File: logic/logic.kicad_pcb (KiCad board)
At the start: 2 copper layers, 32 parts, among them J1 DIN41612_03x32_ABC, J2 Conn_02x05_Odd_Even, J3 Conn_02x05_Odd_Even, J4 Conn_02x05_Odd_Even, U1 TPIC6595, U11 LM7805_TO220, U2 TPIC6595, U3 TPIC6595, U4 TPIC6595, U5 TPIC6595, U6 TPIC6595, U7 TPIC6595, U8 TPIC6595, U9 74HC14

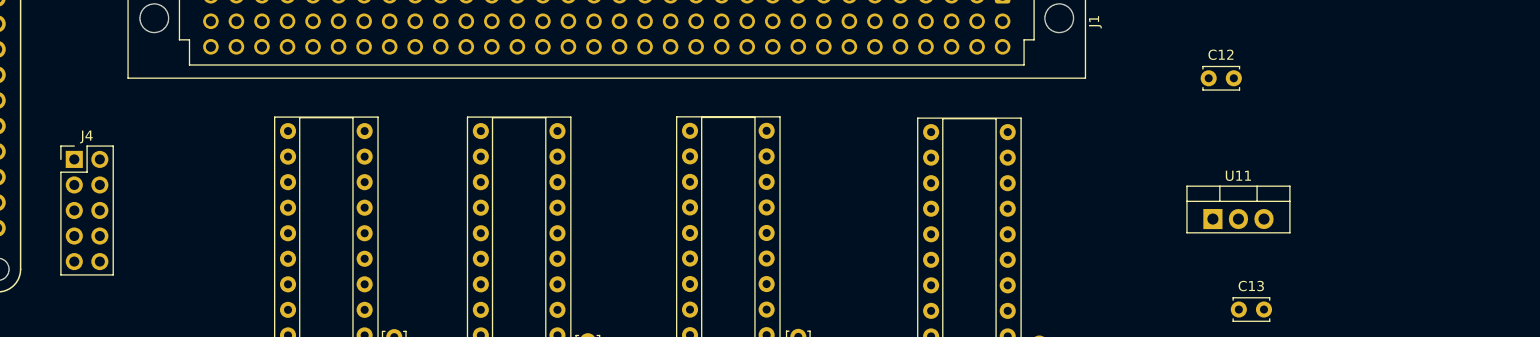
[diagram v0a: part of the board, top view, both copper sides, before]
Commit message: Update libraries, schematic, and layout with buck converter
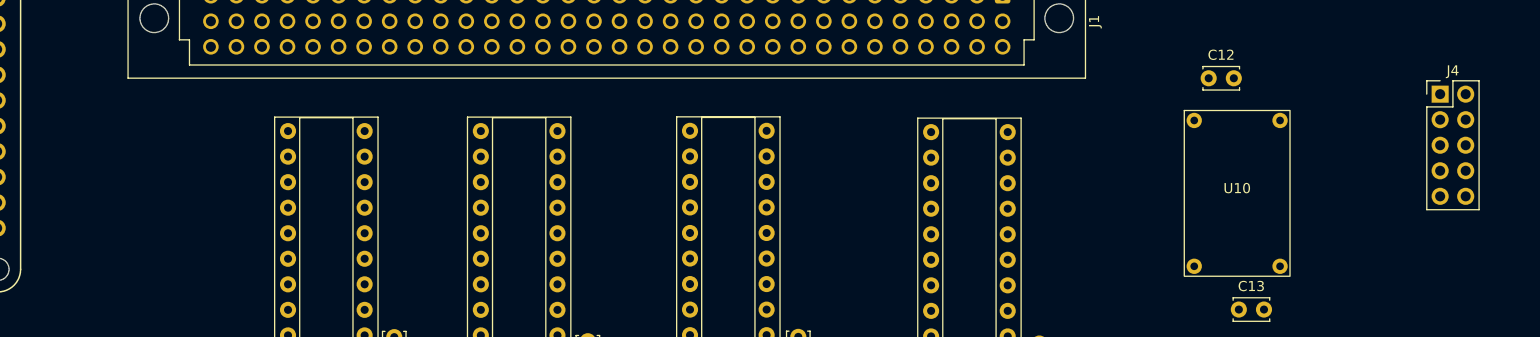
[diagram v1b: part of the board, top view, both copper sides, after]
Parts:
- removed U11: LM7805_TO220, Package_TO_SOT_THT:TO-220-3_Vertical
- added U10: ~, NixComp:TR4R7, F.Cu at (217.3, 90.5)
- moved J4 136.0 mm to (237.5, 80.6)

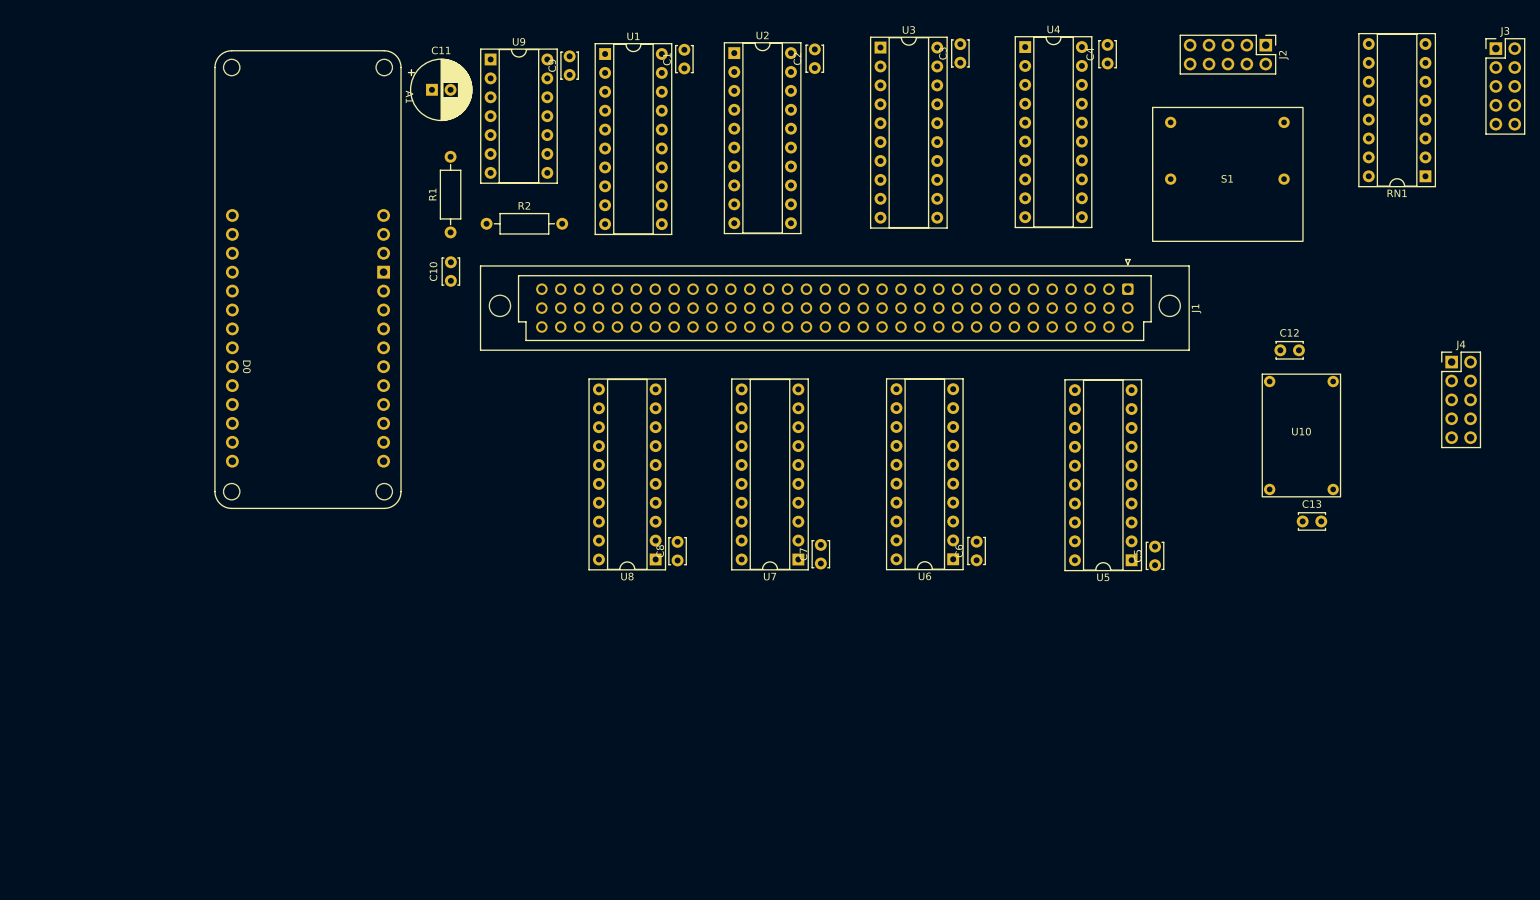
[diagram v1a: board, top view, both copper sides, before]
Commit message: Complete schematic and begin logic board layout.
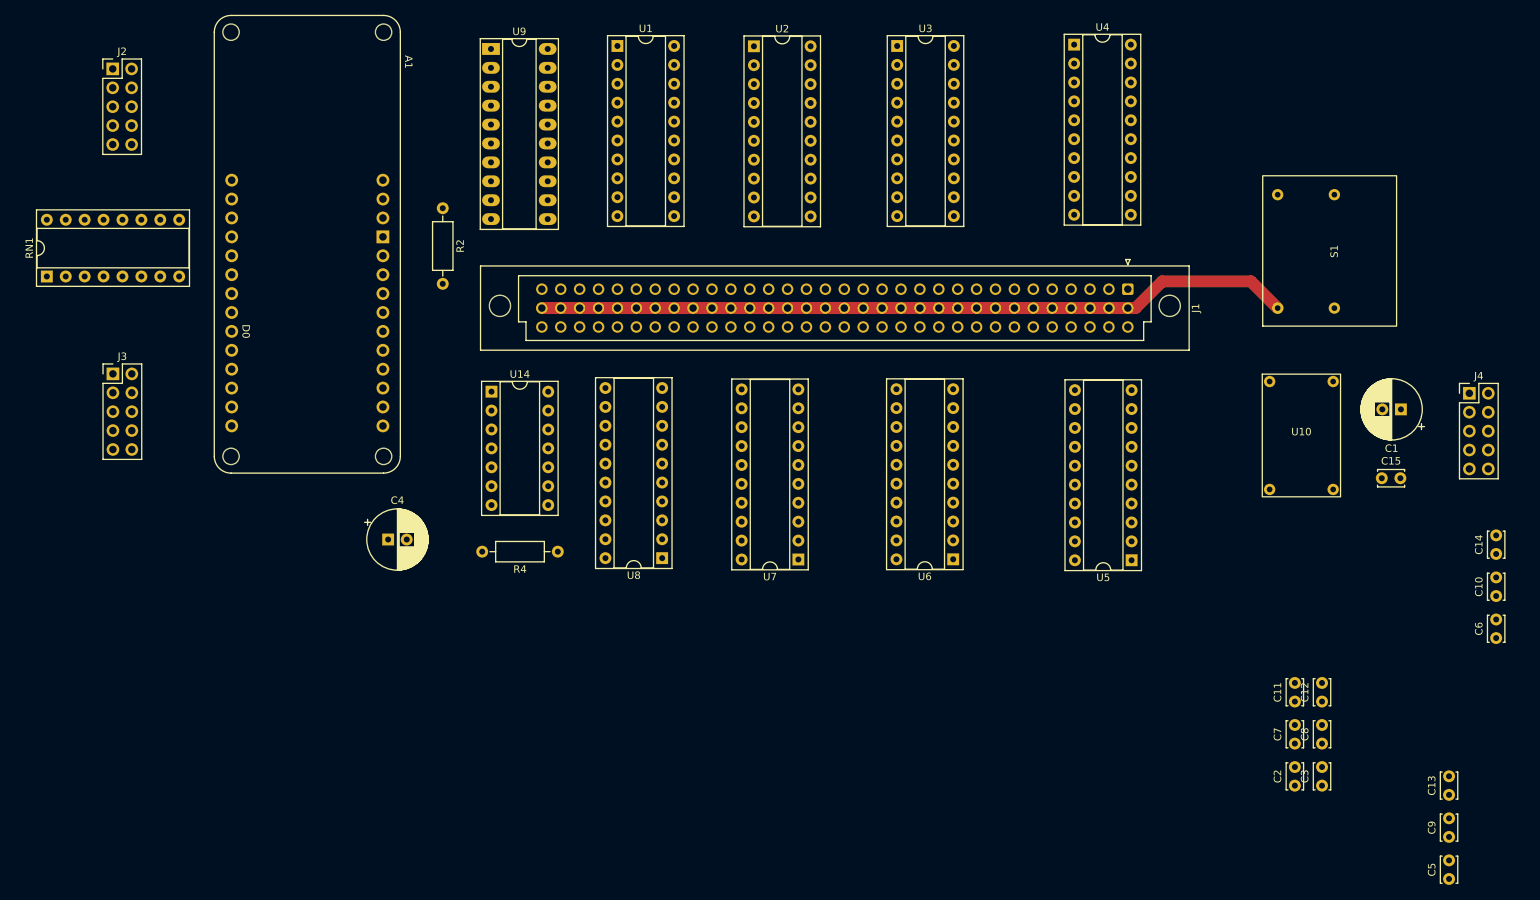
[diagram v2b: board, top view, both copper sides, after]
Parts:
- removed R1: R, Resistor_THT:R_Axial_DIN0207_L6.3mm_D2.5mm_P10.16mm_Horizontal
- added C14: C, Capacitor_THT:C_Disc_D3.4mm_W2.1mm_P2.50mm, F.Cu at (243.5, 106.4)
- added C15: C, Capacitor_THT:C_Disc_D3.4mm_W2.1mm_P2.50mm, F.Cu at (228.1, 96.2)
- added R4: R, Resistor_THT:R_Axial_DIN0207_L6.3mm_D2.5mm_P10.16mm_Horizontal, F.Cu at (117.4, 106.1)
- added U14: 74HC14, Package_DIP:DIP-14_W7.62mm_Socket, F.Cu at (108.5, 84.6)
- C1, C4: footprint Capacitor_THT:C_Disc_D3.4mm_W2.1mm_P2.50mm -> Capacitor_THT:CP_Radial_D8.0mm_P2.50mm
- C11: footprint Capacitor_THT:CP_Radial_D8.0mm_P2.50mm -> Capacitor_THT:C_Disc_D3.4mm_W2.1mm_P2.50mm
- U9: value 74HC14 -> 74HCT244; footprint Package_DIP:DIP-14_W7.62mm_Socket -> Package_DIP:DIP-20_W7.62mm_Socket_LongPads
- moved J3 190.9 mm to (57.6, 82.2)
- moved RN1 185.7 mm to (48.8, 69.1), turned to 90 degrees
- moved C9 156.4 mm to (237.2, 144.4)
- moved J2 155.0 mm to (57.6, 41.2), turned to 0 degrees
- moved C10 146.7 mm to (243.5, 112.0)
- moved C11 142.1 mm to (216.4, 126.2), turned to 90 degrees
- moved C2 116.0 mm to (216.4, 137.5)
- moved C4 115.9 mm to (94.6, 104.4), turned to 0 degrees
- moved C3 108.6 mm to (220.1, 137.5)
- moved C1 106.6 mm to (230.7, 86.9), turned to 180 degrees
- moved C8 90.0 mm to (220.1, 131.8)
- moved C6 70.6 mm to (243.5, 117.7)
- moved C7 68.1 mm to (216.4, 131.8)
- moved C5 57.8 mm to (237.2, 150.0)
- moved C12 47.5 mm to (220.1, 126.2), turned to 90 degrees
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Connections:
- A1 pad 3V3: unconnected-(A1-3.3V-Pad3V3) -> V3.3
- A1 pad 5V: VCC -> unconnected-(A1-Pad5V)
- A1 pad A1: /BT1 -> /~{SRCLR3.3}
- A1 pad A2: /BT2 -> Net-(J2-Pin_1)
- A1 pad A3: /SPARE1 -> Net-(J2-Pin_3)
- A1 pad A4: /SPARE2 -> Net-(J2-Pin_5)
- A1 pad A5: /SW1 -> Net-(J2-Pin_7)
- A1 pad A6: /SW2 -> Net-(J2-Pin_9)
- A1 pad D0: Net-(RN1-R6.1) -> Net-(RN1-R8.1)
- A1 pad D1: Net-(RN1-R5.1) -> Net-(RN1-R7.1)
- A1 pad D2: Net-(RN1-R4.1) -> Net-(RN1-R6.1)
- A1 pad D3: Net-(RN1-R3.1) -> Net-(RN1-R5.1)
- A1 pad D4: Net-(RN1-R2.1) -> Net-(RN1-R4.1)
- A1 pad D5: Net-(RN1-R1.1) -> Net-(RN1-R3.1)
- A1 pad D7: /RCLK -> Net-(U9-I0a)
- A1 pad D8: /COPI -> Net-(A1-D8_MOSI)
- A1 pad D9: /SRCK -> Net-(A1-D9_SCK)
- A1 pad VIN: LV_REG -> V5.0
- C1 pad 1: GND -> Net-(J4-Pin_10)
- C1 pad 2: VCC -> GND
- C10 pad 1: GND -> V5.0
- C10 pad 2: VCC -> GND
- C11 pad 1: Net-(C11-Pad1) -> V5.0
- C12 pad 1: Net-(J4-Pin_10) -> V5.0
- C13 pad 1: LV_REG -> V5.0
- C2 pad 1: GND -> Net-(J4-Pin_10)
- C2 pad 2: VCC -> GND
- C3 pad 1: GND -> V5.0
- C3 pad 2: VCC -> GND
- C4 pad 1: GND -> Net-(C4-Pad1)
- C4 pad 2: VCC -> GND
- C5 pad 1: GND -> V5.0
- C5 pad 2: VCC -> GND
- C6 pad 1: GND -> V5.0
- C6 pad 2: VCC -> GND
- C7 pad 1: GND -> V5.0
- C7 pad 2: VCC -> GND
- C8 pad 1: GND -> V5.0
- C8 pad 2: VCC -> GND
- C9 pad 1: GND -> V5.0
- C9 pad 2: VCC -> GND
- J1 pad a1: unconnected-(J1-Pin_a1-Pada1) -> /B4-0
- J1 pad a10: /B3-6 -> /B3-1
- J1 pad a11: /B3-5 -> /B3-2
- J1 pad a12: /B3-4 -> /B3-3
- J1 pad a13: /B3-3 -> /B3-4
- J1 pad a14: /B3-2 -> /B3-5
- J1 pad a15: /B3-1 -> /B3-6
- J1 pad a16: /B3-0 -> /B3-7
- J1 pad a17: /B2-7 -> /B2-0
- J1 pad a18: /B2-6 -> /B2-1
- J1 pad a19: /B2-5 -> /B2-2
- J1 pad a2: unconnected-(J1-Pin_a2-Pada2) -> /B4-1
- J1 pad a20: /B2-4 -> /B2-3
- J1 pad a21: /B2-3 -> /B2-4
- J1 pad a22: /B2-2 -> /B2-5
- J1 pad a23: /B2-1 -> /B2-6
- J1 pad a24: /B2-0 -> /B2-7
- J1 pad a25: /B1-7 -> /B1-0
- J1 pad a26: /B1-6 -> /B1-1
- J1 pad a27: /B1-5 -> /B1-2
- J1 pad a28: /B1-4 -> /B1-3
- J1 pad a29: /B1-3 -> /B1-4
- J1 pad a3: /B4-5 -> /B4-2
- J1 pad a30: /B1-2 -> /B1-5
- J1 pad a31: /B1-1 -> /B1-6
- J1 pad a32: /B1-0 -> /B1-7
- J1 pad a4: /B4-4 -> /B4-3
- J1 pad a5: /B4-3 -> /B4-4
- J1 pad a6: /B4-2 -> /B4-5
- J1 pad a7: /B4-1 -> /B4-6
- J1 pad a8: /B4-0 -> /B4-7
- J1 pad a9: /B3-7 -> /B3-0
- J1 pad b1: Net-(J1-Pin_b1) -> V170
- J1 pad b10: Net-(J1-Pin_b1) -> V170
- J1 pad b11: Net-(J1-Pin_b1) -> V170
- J1 pad b12: Net-(J1-Pin_b1) -> V170
- J1 pad b13: Net-(J1-Pin_b1) -> V170
- J1 pad b14: Net-(J1-Pin_b1) -> V170
- J1 pad b15: Net-(J1-Pin_b1) -> V170
- J1 pad b16: Net-(J1-Pin_b1) -> V170
- J1 pad b17: Net-(J1-Pin_b1) -> V170
- J1 pad b18: Net-(J1-Pin_b1) -> V170
- J1 pad b19: Net-(J1-Pin_b1) -> V170
- J1 pad b2: Net-(J1-Pin_b1) -> V170
- J1 pad b20: Net-(J1-Pin_b1) -> V170
- J1 pad b21: Net-(J1-Pin_b1) -> V170
- J1 pad b22: Net-(J1-Pin_b1) -> V170
- J1 pad b23: Net-(J1-Pin_b1) -> V170
- J1 pad b24: Net-(J1-Pin_b1) -> V170
- J1 pad b25: Net-(J1-Pin_b1) -> V170
- J1 pad b26: Net-(J1-Pin_b1) -> V170
- J1 pad b27: Net-(J1-Pin_b1) -> V170
- J1 pad b28: Net-(J1-Pin_b1) -> V170
- J1 pad b29: Net-(J1-Pin_b1) -> V170
- J1 pad b3: Net-(J1-Pin_b1) -> V170
- J1 pad b30: Net-(J1-Pin_b1) -> V170
- J1 pad b31: Net-(J1-Pin_b1) -> V170
- J1 pad b32: Net-(J1-Pin_b1) -> V170
- J1 pad b4: Net-(J1-Pin_b1) -> V170
- J1 pad b5: Net-(J1-Pin_b1) -> V170
- J1 pad b6: Net-(J1-Pin_b1) -> V170
- J1 pad b7: Net-(J1-Pin_b1) -> V170
- J1 pad b8: Net-(J1-Pin_b1) -> V170
- J1 pad b9: Net-(J1-Pin_b1) -> V170
- J1 pad c31: unconnected-(J1-Pin_c31-Padc31) -> /B8-6
- J1 pad c32: unconnected-(J1-Pin_c32-Padc32) -> /B8-7
- J2 pad 1: VCC -> Net-(J2-Pin_1)
- J2 pad 10: /SPARE2 -> GND
- J2 pad 3: VCC -> Net-(J2-Pin_3)
- J2 pad 5: /BT1 -> Net-(J2-Pin_5)
- J2 pad 6: /SW2 -> GND
- J2 pad 7: /BT2 -> Net-(J2-Pin_7)
- J2 pad 8: /SW1 -> GND
- J2 pad 9: /SPARE1 -> Net-(J2-Pin_9)
- J3 pad 10: VCC -> V3.3
- J3 pad 7: GND -> V3.3
- J3 pad 8: VCC -> V3.3
- J3 pad 9: GND -> V3.3
- R2 pad 1: VCC -> V3.3
- RN1 pad 1: Net-(RN1-R1.1) -> unconnected-(RN1-R1.1-Pad1)
- RN1 pad 10: unconnected-(RN1-R7.2-Pad10) -> Net-(J3-Pin_4)
- RN1 pad 11: Net-(J3-Pin_6) -> Net-(J3-Pin_2)
- RN1 pad 12: Net-(J3-Pin_4) -> Net-(J3-Pin_1)
- RN1 pad 13: Net-(J3-Pin_2) -> Net-(J3-Pin_3)
- RN1 pad 14: Net-(J3-Pin_1) -> Net-(J3-Pin_5)
- RN1 pad 15: Net-(J3-Pin_3) -> unconnected-(RN1-R2.2-Pad15)
- RN1 pad 16: Net-(J3-Pin_5) -> unconnected-(RN1-R1.2-Pad16)
- RN1 pad 2: Net-(RN1-R2.1) -> unconnected-(RN1-R2.1-Pad2)
- RN1 pad 7: unconnected-(RN1-R7.1-Pad7) -> Net-(RN1-R7.1)
- RN1 pad 8: unconnected-(RN1-R8.1-Pad8) -> Net-(RN1-R8.1)
- RN1 pad 9: unconnected-(RN1-R8.2-Pad9) -> Net-(J3-Pin_6)
- S1 pad 1: VCC -> V170
- S1 pad 2: GND -> V5.0
- S1 pad 4: Net-(J1-Pin_b1) -> GND
- U1 pad 2: VCC -> V5.0
- U1 pad 8: VCC -> /~{SRCLR}
- U1 pad 9: /~{POR} -> POR
- U10 pad 2: LV_REG -> V5.0
- U2 pad 2: VCC -> V5.0
- U2 pad 8: VCC -> /~{SRCLR}
- U2 pad 9: /~{POR} -> POR
- U3 pad 2: VCC -> V5.0
- U3 pad 8: VCC -> /~{SRCLR}
- U3 pad 9: /~{POR} -> POR
- U4 pad 16: unconnected-(U4-DRAIN6-Pad16) -> /B4-6
- U4 pad 17: unconnected-(U4-DRAIN7-Pad17) -> /B4-7
- U4 pad 2: VCC -> V5.0
- U4 pad 8: VCC -> /~{SRCLR}
- U4 pad 9: /~{POR} -> POR
- U5 pad 2: VCC -> V5.0
- U5 pad 8: VCC -> /~{SRCLR}
- U5 pad 9: /~{POR} -> POR
- U6 pad 2: VCC -> V5.0
- U6 pad 8: VCC -> /~{SRCLR}
- U6 pad 9: /~{POR} -> POR
- U7 pad 2: VCC -> V5.0
- U7 pad 8: VCC -> /~{SRCLR}
- U7 pad 9: /~{POR} -> POR
- U8 pad 16: unconnected-(U8-DRAIN6-Pad16) -> /B8-6
- U8 pad 17: unconnected-(U8-DRAIN7-Pad17) -> /B8-7
- U8 pad 2: VCC -> V5.0
- U8 pad 8: VCC -> /~{SRCLR}
- U8 pad 9: /~{POR} -> POR
- U9 pad 1: Net-(C11-Pad1) -> GND
- U9 pad 10: unconnected-(U9-Pad10) -> GND
- U9 pad 12: /~{POR} -> /~{SRCLR}
- U9 pad 13: Net-(U9-Pad13) -> GND
- U9 pad 14: VCC -> /SRCK
- U9 pad 2: Net-(U9-Pad13) -> Net-(U9-I0a)
- U9 pad 3: GND -> unconnected-(U9-O3b-Pad3)
- U9 pad 4: unconnected-(U9-Pad4) -> Net-(A1-D8_MOSI)
- U9 pad 5: GND -> unconnected-(U9-O2b-Pad5)
- U9 pad 6: unconnected-(U9-Pad6) -> Net-(A1-D9_SCK)
- U9 pad 7: GND -> unconnected-(U9-O1b-Pad7)
- U9 pad 8: unconnected-(U9-Pad8) -> /~{SRCLR3.3}
- U9 pad 9: GND -> unconnected-(U9-O0b-Pad9)
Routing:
- net V170: track 0.00 -> 101.8 mm

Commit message: Ongoing development. Add shunt resistors to display board.
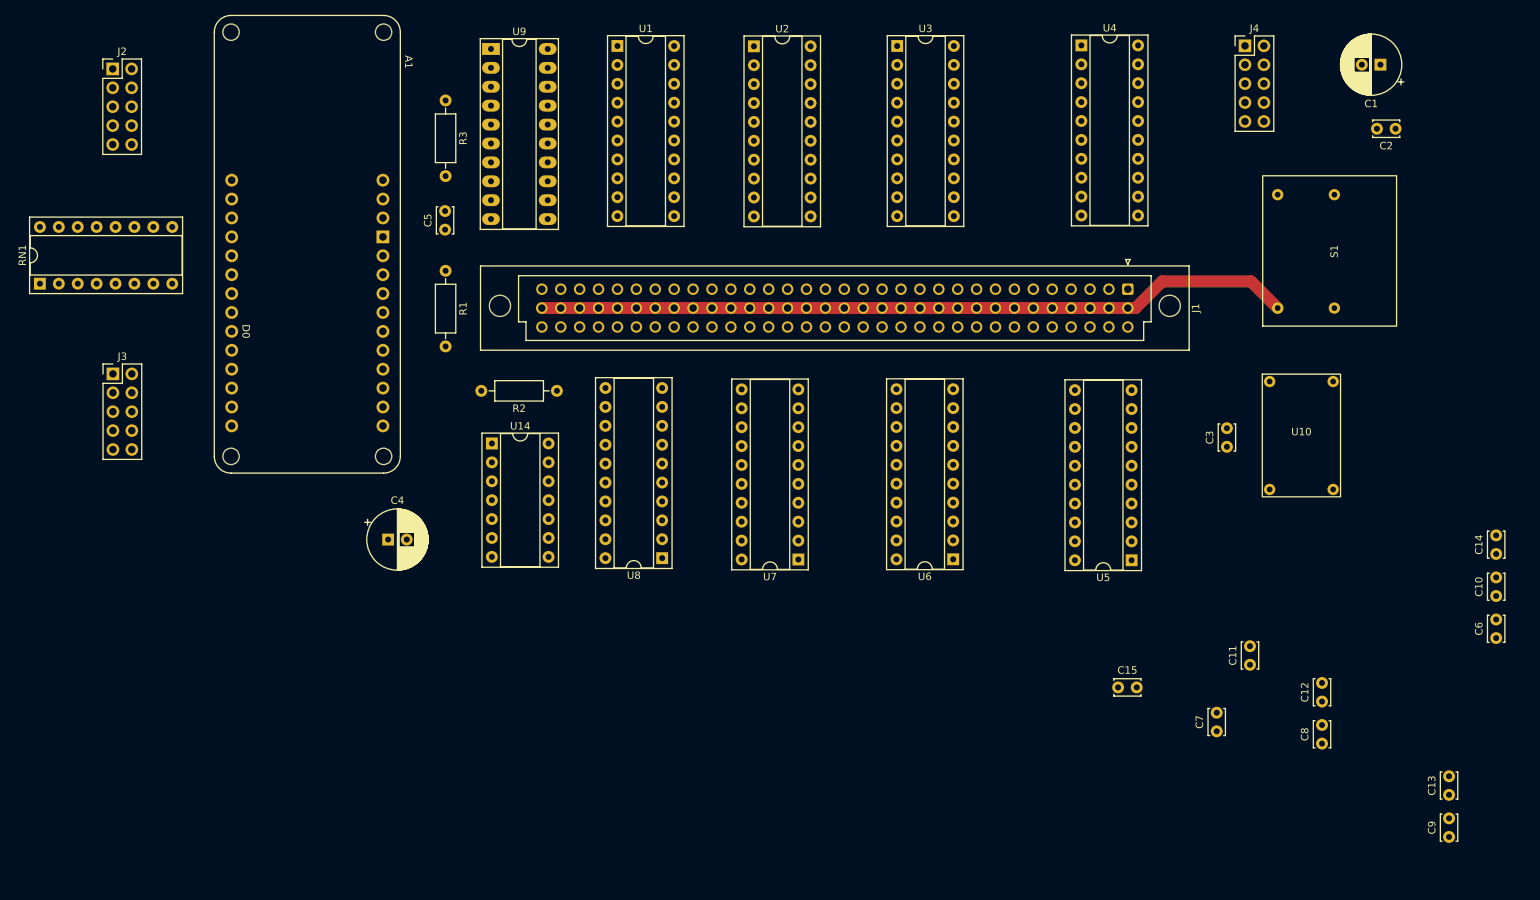
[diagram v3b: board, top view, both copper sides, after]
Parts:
- removed R4: R, Resistor_THT:R_Axial_DIN0207_L6.3mm_D2.5mm_P10.16mm_Horizontal
- added R1: R, Resistor_THT:R_Axial_DIN0207_L6.3mm_D2.5mm_P10.16mm_Horizontal, F.Cu at (102.3, 68.3)
- added R3: R, Resistor_THT:R_Axial_DIN0207_L6.3mm_D2.5mm_P10.16mm_Horizontal, F.Cu at (102.3, 45.4)
- moved C5 160.7 mm to (102.3, 62.8)
- moved C2 89.3 mm to (230.0, 49.2), turned to 180 degrees
- moved J4 55.6 mm to (209.8, 38.1)
- moved C3 47.3 mm to (207.3, 92.0)
- moved C1 46.4 mm to (227.9, 40.6)
- moved C15 45.2 mm to (192.7, 124.3)
- moved R2 28.9 mm to (117.3, 84.5), turned to 180 degrees
- moved C7 10.6 mm to (205.9, 130.2)
- moved C11 7.80 mm to (210.4, 121.3)
- moved U14 6.96 mm to (108.5, 91.5)
- moved RN1 1.34 mm to (47.8, 70.0)
- moved U4 0.98 mm to (187.8, 38.0)
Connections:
- R2 pad 1: V3.3 -> V5.0
- R2 pad 2: Net-(A1-RESET) -> Net-(C4-Pad1)

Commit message: Ongoing development
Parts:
- U1, U2, U3, U4, U5, U6, U7, U8: footprint Package_DIP:DIP-20_W7.62mm_Socket -> Package_DIP:DIP-20_W7.62mm_Socket_LongPads
- U14: footprint Package_DIP:DIP-14_W7.62mm_Socket -> Package_DIP:DIP-14_W7.62mm_Socket_LongPads
- moved C6 130.6 mm to (127.0, 58.7)
- moved C7 104.2 mm to (130.1, 58.7)
- moved RN1 66.9 mm to (94.5, 118.0), turned to -90 degrees
- moved C10 56.3 mm to (187.2, 112.5)
- moved C14 56.3 mm to (187.2, 106.9)
- moved C9 54.1 mm to (186.7, 124.9)
- moved C13 53.7 mm to (187.3, 118.8)
- moved C1 51.0 mm to (219.1, 90.9)
- moved C2 45.5 mm to (210.2, 90.2), turned to -90 degrees
- moved R1 35.1 mm to (109.9, 102.6)
- moved C3 26.3 mm to (207.8, 118.3)
- moved J3 25.3 mm to (74.1, 101.3)
- moved C15 25.2 mm to (217.1, 118.3)
- moved J2 24.1 mm to (73.7, 59.1)
- moved J4 21.2 mm to (207.8, 59.2), turned to 90 degrees
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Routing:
- net V170: track 101.8 -> 0.00 mm
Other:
- board outline added: 157 x 79.4 mm
